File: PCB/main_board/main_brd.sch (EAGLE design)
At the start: 29 parts, among them J1 MS5803_14BA Break_out, J2 SD-card Adapter, J3 E-paper Module, J4 Zigbee Module, J5 BATT, J6 CHARGER, J7 POGO_PINS, J8 ST-LINK, U1 STM32F103C8T6-MODULE

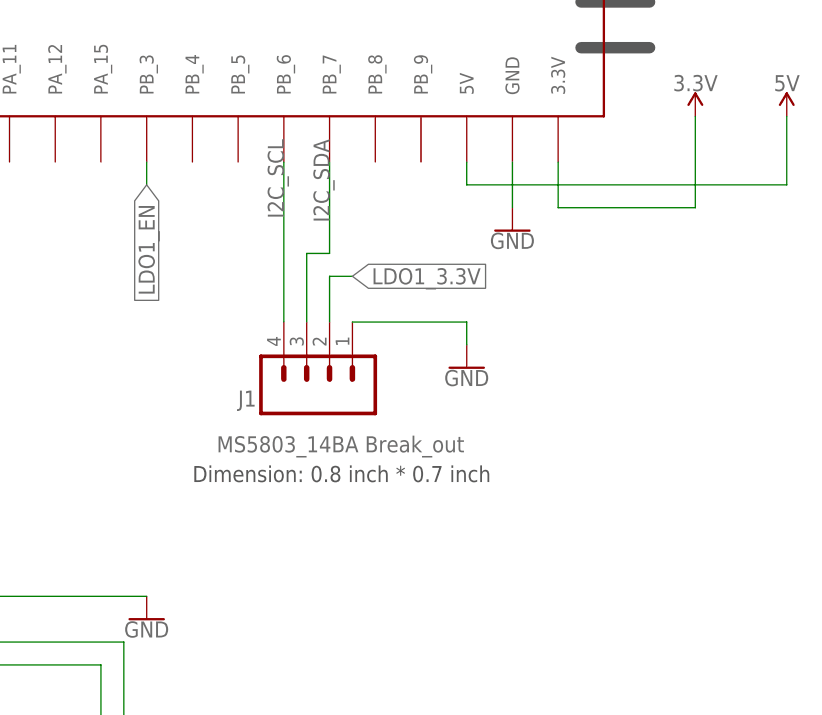
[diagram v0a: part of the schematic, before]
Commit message: added I2C bus to the schematic and did the routing for the PCB board
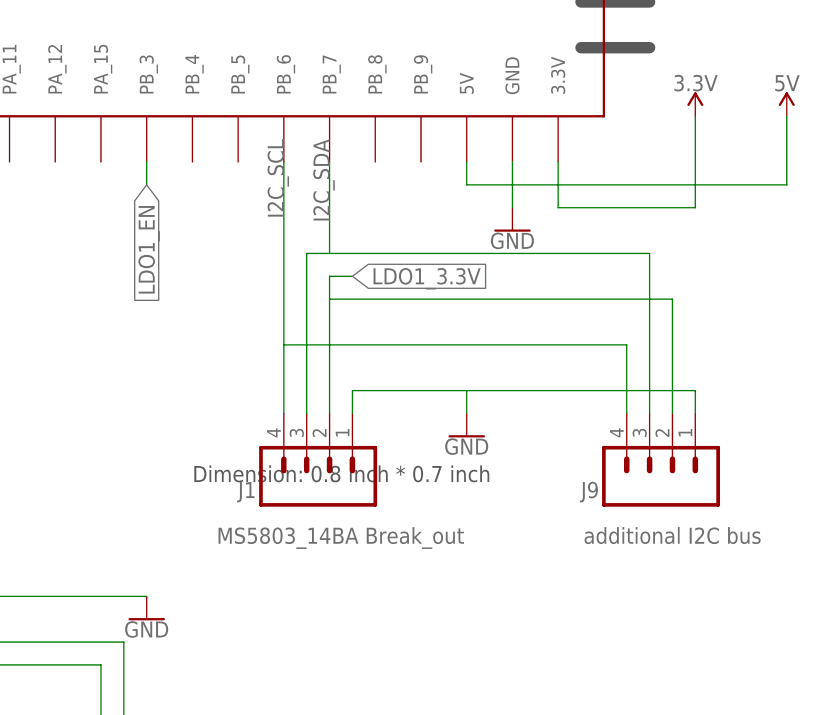
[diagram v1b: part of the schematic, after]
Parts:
- added J9: additional I2C bus, SparkFun-Connectors:CONN_04PTH
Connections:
- net GND: now also J9.1
- net I2C_SCL: now also J9.4
- net I2C_SDA: now also J9.3
- net LDO1_3.3V: now also J9.2
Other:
- moved on the sheet: J1
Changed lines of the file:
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@@
 <?xml version="1.0" encoding="utf-8"?>
 <!DOCTYPE eagle SYSTEM "eagle.dtd">
-<eagle version="9.3.2">
+<eagle version="9.2.2">
 <drawing>
 <settings>
@@
 <part name="GND15" library="SparkFun-PowerSymbols" deviceset="GND" device=""/>
 <part name="J8" library="SparkFun-Connectors" deviceset="CONN_02" device="" value="ST-LINK"/>
+<part name="J9" library="SparkFun-Connectors" deviceset="CONN_04" device="PTH" value="additional I2C bus"/>
 </parts>
 <sheets>
@@
 <attribute name="VALUE" x="302.26" y="177.8" size="1.778" layer="96"/>
 </instance>
-<instance part="J1" gate="J1" x="342.9" y="134.62" smashed="yes" rot="R90">
-<attribute name="VALUE" x="357.886" y="127" size="1.778" layer="96" font="vector" rot="R180"/>
-<attribute name="NAME" x="334.772" y="132.08" size="1.778" layer="95" font="vector" rot="R180"/>
+<instance part="J1" gate="J1" x="342.9" y="124.46" smashed="yes" rot="R90">
+<attribute name="VALUE" x="357.886" y="116.84" size="1.778" layer="96" font="vector" rot="R180"/>
+<attribute name="NAME" x="334.772" y="121.92" size="1.778" layer="95" font="vector" rot="R180"/>
 </instance>
 <instance part="J2" gate="G$1" x="251.46" y="137.16" smashed="yes">
@@
 <attribute name="VALUE" x="365.76" y="213.868" size="1.778" layer="96" font="vector" align="top-center"/>
 </instance>
-<instance part="GND1" gate="1" x="358.14" y="134.62" smashed="yes">
-<attribute name="VALUE" x="358.14" y="134.366" size="1.778" layer="96" align="top-center"/>
+<instance part="GND1" gate="1" x="358.14" y="127" smashed="yes">
+<attribute name="VALUE" x="358.14" y="126.746" size="1.778" layer="96" align="top-center"/>
 </instance>
 <instance part="GND2" gate="1" x="261.62" y="119.38" smashed="yes">
@@
 <attribute name="NAME" x="342.9" y="91.948" size="1.778" layer="95" font="vector" rot="MR0"/>
 </instance>
+<instance part="J9" gate="J1" x="381" y="124.46" smashed="yes" rot="R90">
+<attribute name="VALUE" x="390.906" y="116.84" size="1.778" layer="96" font="vector" rot="R180"/>
+<attribute name="NAME" x="372.872" y="121.92" size="1.778" layer="95" font="vector" rot="R180"/>
+</instance>
 </instances>
 <busses>
@@
 <net name="GND" class="0">
 <segment>
+<pinref part="GND1" gate="1" pin="GND"/>
+<wire x1="358.14" y1="132.08" x2="358.14" y2="129.54" width="0.1524" layer="91"/>
+<wire x1="358.14" y1="132.08" x2="383.54" y2="132.08" width="0.1524" layer="91"/>
+<pinref part="J9" gate="J1" pin="1"/>
+<wire x1="383.54" y1="132.08" x2="383.54" y2="129.54" width="0.1524" layer="91"/>
 <pinref part="J1" gate="J1" pin="1"/>
-<pinref part="GND1" gate="1" pin="GND"/>
-<wire x1="345.44" y1="139.7" x2="358.14" y2="139.7" width="0.1524" layer="91"/>
-<wire x1="358.14" y1="139.7" x2="358.14" y2="137.16" width="0.1524" layer="91"/>
+<wire x1="345.44" y1="129.54" x2="345.44" y2="132.08" width="0.1524" layer="91"/>
+<wire x1="345.44" y1="132.08" x2="358.14" y2="132.08" width="0.1524" layer="91"/>
 </segment>
 <segment>
@@
 <wire x1="342.9" y1="147.32" x2="340.36" y2="147.32" width="0.1524" layer="91"/>
 <pinref part="J1" gate="J1" pin="3"/>
-<wire x1="340.36" y1="147.32" x2="340.36" y2="139.7" width="0.1524" layer="91"/>
+<wire x1="340.36" y1="147.32" x2="340.36" y2="129.54" width="0.1524" layer="91"/>
+<wire x1="342.9" y1="147.32" x2="378.46" y2="147.32" width="0.1524" layer="91"/>
+<pinref part="J9" gate="J1" pin="3"/>
+<wire x1="378.46" y1="147.32" x2="378.46" y2="129.54" width="0.1524" layer="91"/>
 </segment>
 </net>
@@
 <label x="337.82" y="160.02" size="1.778" layer="95" rot="MR270"/>
 <pinref part="J1" gate="J1" pin="4"/>
-<wire x1="337.82" y1="157.48" x2="337.82" y2="139.7" width="0.1524" layer="91"/>
+<wire x1="337.82" y1="157.48" x2="337.82" y2="137.16" width="0.1524" layer="91"/>
+<pinref part="J9" gate="J1" pin="4"/>
+<wire x1="337.82" y1="137.16" x2="337.82" y2="129.54" width="0.1524" layer="91"/>
+<wire x1="337.82" y1="137.16" x2="375.92" y2="137.16" width="0.1524" layer="91"/>
+<wire x1="375.92" y1="137.16" x2="375.92" y2="129.54" width="0.1524" layer="91"/>
 </segment>
 </net>
@@
 <segment>
 <pinref part="J1" gate="J1" pin="2"/>
-<wire x1="342.9" y1="139.7" x2="342.9" y2="144.78" width="0.1524" layer="91"/>
+<wire x1="342.9" y1="129.54" x2="342.9" y2="142.24" width="0.1524" layer="91"/>
+<wire x1="342.9" y1="142.24" x2="342.9" y2="144.78" width="0.1524" layer="91"/>
 <wire x1="342.9" y1="144.78" x2="345.44" y2="144.78" width="0.1524" layer="91"/>
 <label x="345.44" y="144.78" size="1.778" layer="95" xref="yes"/>
-</segment>
-<segment>
+<wire x1="342.9" y1="142.24" x2="381" y2="142.24" width="0.1524" layer="91"/>
+<pinref part="J9" gate="J1" pin="2"/>
+<wire x1="381" y1="142.24" x2="381" y2="129.54" width="0.1524" layer="91"/>
+</segment>
+<segment>

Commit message: finalized PCB and updated the Voltage reading methodology
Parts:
- added C8: UWT1C221MCL1GSU2-K-M, capacitor_220uF:UWT1C221MCL1GSU2-K-M
- added TP1, TP2, TP3, TP4, TP5, TP6, TP7, TP8: TEST-POINT3X5, SparkFun-Connectors:TEST-POINT3X5
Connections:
- removed net 5V: U$2.5V, U1.5V
- new net +5V: C1.1, C4.1, LDO1.VIN, LDO2.VIN, TP1.1, U$2.5V, U1.5V
- net 3.3V: no longer C1.1, C4.1, LDO1.VIN, LDO2.VIN
- net GND: now also C8.2
- net I2C_SCL: now also TP3.1
- net I2C_SDA: now also TP2.1
- net LDO1_3.3V: now also TP4.1
- net LDO1_EN: now also U1.PB_0; no longer U1.PB_3
- net LDO2_3.3V: now also TP5.1
- net LDO2_EN: now also U1.PB_3; no longer U1.PB_0
- net SPI1_MOSI: now also TP6.1
- net SPI1_NSS/CS: now also TP8.1
- net SPI1_SCK: now also TP7.1
- net V_CHARGE: now also C8.1
